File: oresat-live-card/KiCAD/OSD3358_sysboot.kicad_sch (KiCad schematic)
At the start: 7 parts, among them J3 Conn_01x02, U7 OSD3358-512M-BSM

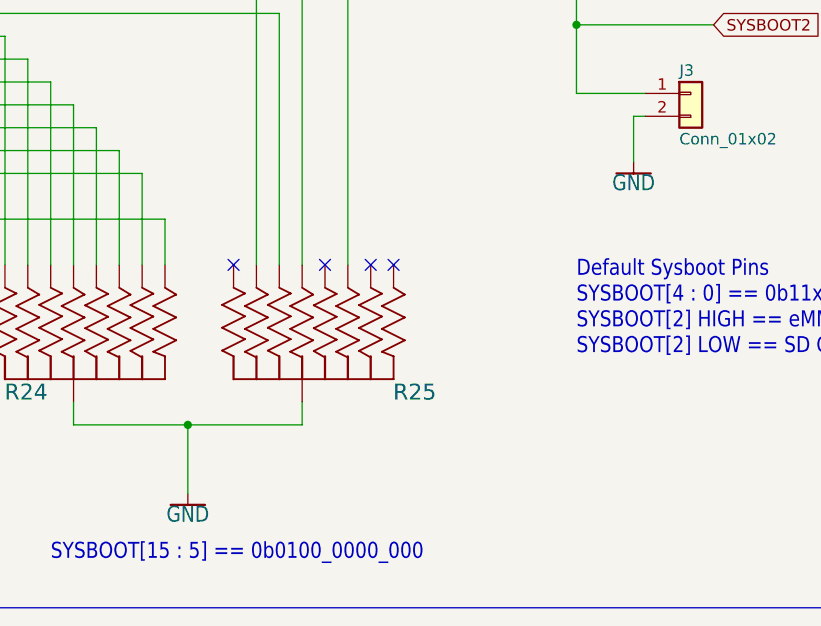
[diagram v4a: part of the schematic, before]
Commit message: completed tx/rx switch circuit and cleaned up GND references
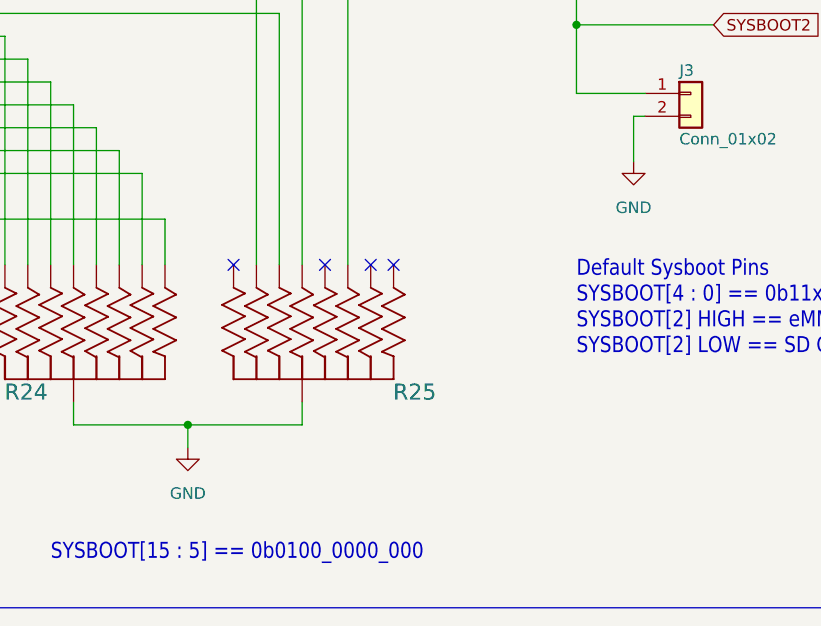
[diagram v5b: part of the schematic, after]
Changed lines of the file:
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@@
 		(title "Oresat DxWifi Card")
 		(date "2024-01-02")
-		(rev "1.3")
+		(rev "2")
 	)
 	(text "0"
@@
 	(wire
 		(pts
-			(xy 210.82 176.53) (xy 210.82 184.15)
+			(xy 210.82 176.53) (xy 210.82 179.07)
 		)
 		(stroke
@@
 	)
 	(symbol
-		(lib_id "oresat-power:GND")
-		(at 260.35 147.32 0)
-		(mirror y)
-		(unit 1)
-		(exclude_from_sim no)
-		(in_bom yes)
-		(on_board yes)
-		(dnp no)
-		(property "Reference" "#GND034"
-			(at 260.35 147.32 0)
-			(effects
-				(font
-					(size 1.27 1.27)
-				)
-				(hide yes)
-			)
-		)
-		(property "Value" "GND"
-			(at 260.35 148.59 0)
-			(effects
-				(font
-					(size 1.778 1.5113)
-				)
-				(justify top)
-			)
-		)
-		(property "Footprint" "oresat-live-card:"
-			(at 260.35 147.32 0)
-			(effects
-				(font
-					(size 1.27 1.27)
-				)
-				(hide yes)
-			)
-		)
-		(property "Datasheet" ""
-			(at 260.35 147.32 0)
-			(effects
-				(font
-					(size 1.27 1.27)
-				)
-				(hide yes)
-			)
-		)
-		(property "Description" ""
-			(at 260.35 147.32 0)
-			(effects
-				(font
-					(size 1.27 1.27)
-				)
-				(hide yes)
-			)
-		)
-		(pin "1"
-		)
-		(instances
-			(project "oresat-live-card"
-				(path "/748bdd2d-da0a-4240-ba60-0bf881d2ec56/70b8c0f4-d0a6-4f08-9b41-fcc84e804ec9"
-					(reference "#GND034")
-					(unit 1)
-				)
-			)
-		)
-	)
-	(symbol
 		(lib_id "oresat-passives:EXB-A10P391J")
 		(at 208.28 171.45 270)
@@
 	)
 	(symbol
-		(lib_id "oresat-power:GND")
-		(at 210.82 184.15 0)
-		(mirror y)
+		(lib_id "power:GND")
+		(at 260.35 147.32 0)
 		(unit 1)
 		(exclude_from_sim no)
@@
 		(on_board yes)
 		(dnp no)
-		(property "Reference" "#GND0112"
-			(at 210.82 184.15 0)
+		(fields_autoplaced yes)
+		(property "Reference" "#PWR051"
+			(at 260.35 153.67 0)
 			(effects
 				(font
@@
 		)
 		(property "Value" "GND"
-			(at 210.82 185.42 0)
-			(effects
-				(font
-					(size 1.778 1.5113)
-				)
-				(justify top)
-			)
-		)
-		(property "Footprint" "oresat-live-card:"
-			(at 210.82 184.15 0)
+			(at 260.35 152.4 0)
+			(effects
+				(font
+					(size 1.27 1.27)
+				)
+			)
+		)
+		(property "Footprint" ""
+			(at 260.35 147.32 0)
 			(effects
 				(font
@@
 		)
 		(property "Datasheet" ""
-			(at 210.82 184.15 0)
-			(effects
-				(font
-					(size 1.27 1.27)
-				)
-				(hide yes)
-			)
-		)
-		(property "Description" ""
-			(at 210.82 184.15 0)
+			(at 260.35 147.32 0)
+			(effects
+				(font
+					(size 1.27 1.27)
+				)
+				(hide yes)
+			)
+		)
+		(property "Description" "Power symbol creates a global label with name \"GND\" , ground"
+			(at 260.35 147.32 0)
 			(effects
 				(font
@@
 			(project "oresat-live-card"
 				(path "/748bdd2d-da0a-4240-ba60-0bf881d2ec56/70b8c0f4-d0a6-4f08-9b41-fcc84e804ec9"
-					(reference "#GND0112")
+					(reference "#PWR051")
 					(unit 1)
 				)
+			)
+		)
+	)
+	(symbol
+		(lib_id "power:GND")
+		(at 210.82 179.07 0)
+		(unit 1)
+		(exclude_from_sim no)
+		(in_bom yes)
+		(on_board yes)
+		(dnp no)
+		(fields_autoplaced yes)
+		(property "Reference" "#PWR050"
+			(at 210.82 185.42 0)
+			(effects
+				(font
+					(size 1.27 1.27)
+				)
+				(hide yes)
+			)
+		)
+		(property "Value" "GND"
+			(at 210.82 184.15 0)
+			(effects
+				(font
+					(size 1.27 1.27)
+				)
+			)
+		)
+		(property "Footprint" ""
+			(at 210.82 179.07 0)
+			(effects
+				(font
+					(size 1.27 1.27)
+				)
+				(hide yes)
+			)
+		)
+		(property "Datasheet" ""
+			(at 210.82 179.07 0)
+			(effects
+				(font
+					(size 1.27 1.27)
+				)
+				(hide yes)
+			)
+		)
+		(property "Description" "Power symbol creates a global label with name \"GND\" , ground"
+			(at 210.82 179.07 0)
+			(effects
+				(font
+					(size 1.27 1.27)
+				)
+				(hide yes)
+			)
+		)
+		(pin "1"
+		)
+		(instances
+			(project "oresat-live-card"
+				(path "/748bdd2d-da0a-4240-ba60-0bf881d2ec56/70b8c0f4-d0a6-4f08-9b41-fcc84e804ec9"
+					(reference "#PWR050")
+					(unit 1)
+				)

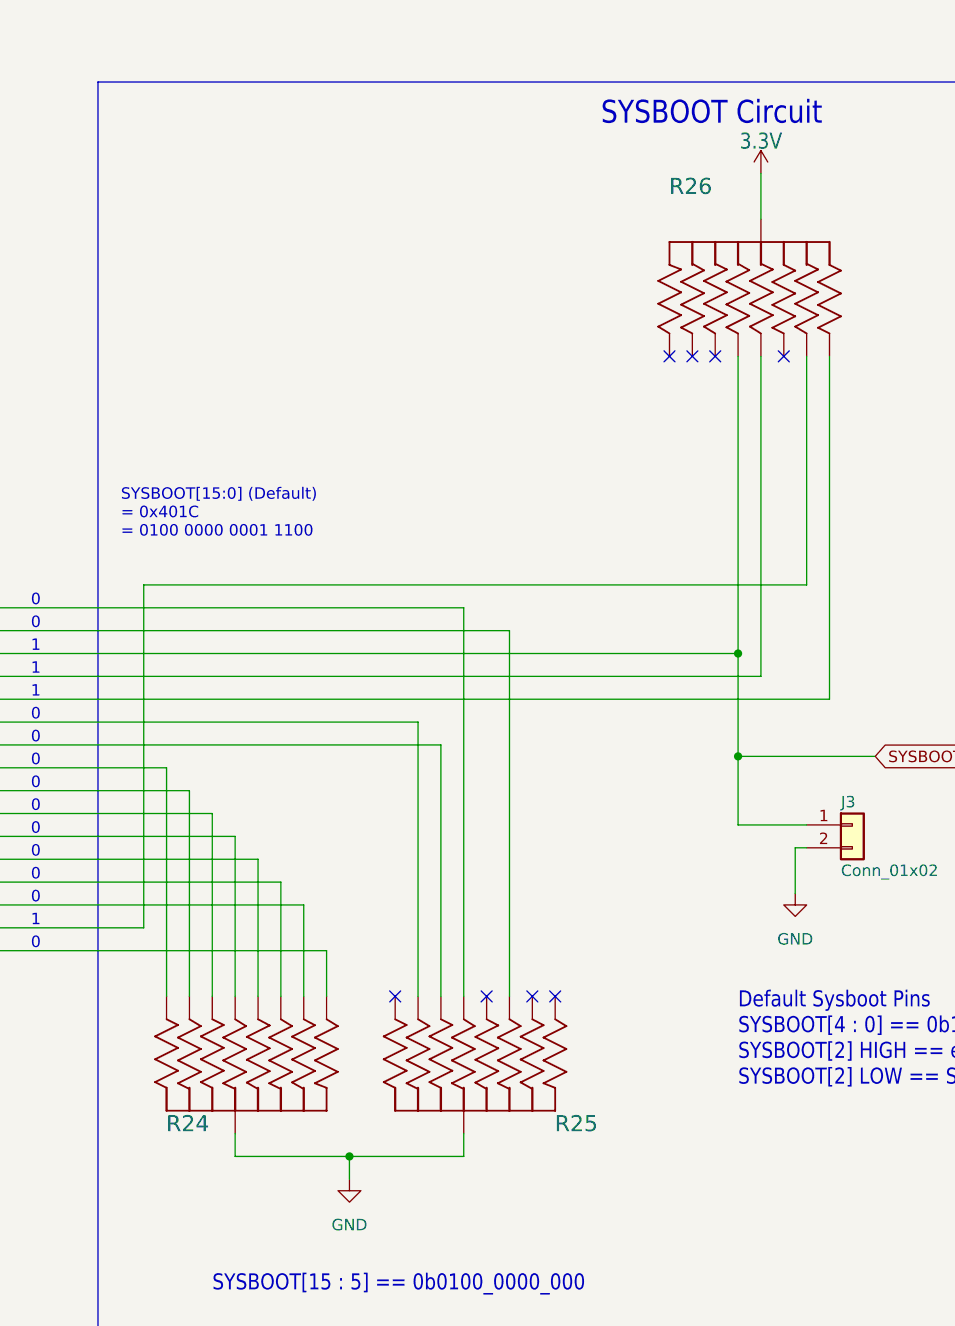
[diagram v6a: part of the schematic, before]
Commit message: Fixed up schematic as best as possible. There were a lot of issues with local paths being referenced, and EAGLE import libraries. Fixed all of those, as well as fixed some oresat-kicad IC symbols (bad direction pins) and I think we're now OK. Also updated card outline for two RF (LEFT) connectors.  Still missing two packages, but we'll deal with that later.
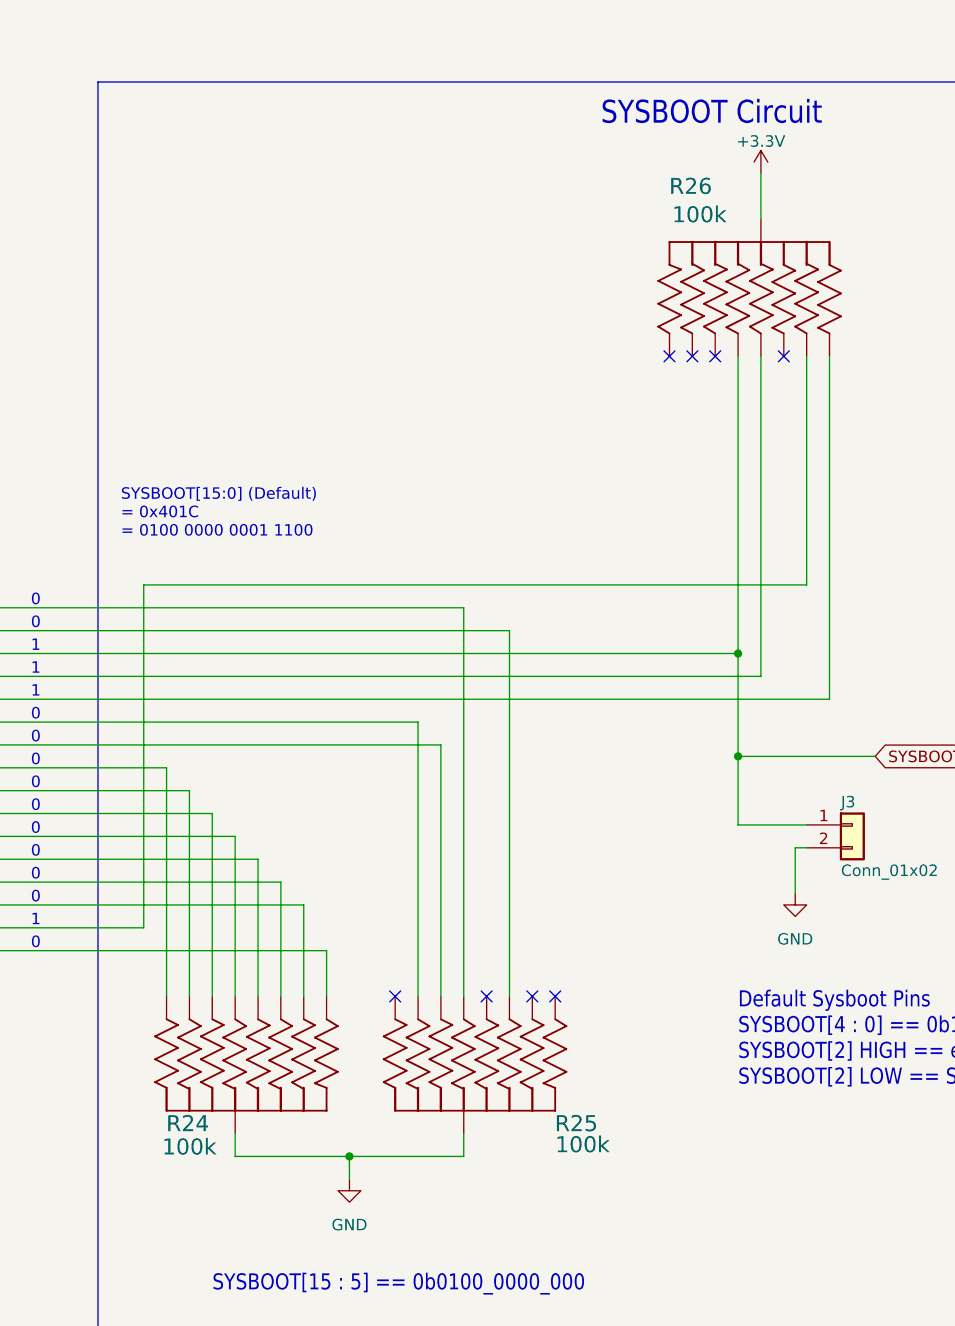
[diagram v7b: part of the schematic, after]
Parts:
- R24, R25, R26: value EXB-A10P104J -> 100k; DPN (none) -> U7104CT-ND; MFR (none) -> Panasonic
- U7: DPN (none) -> 1676-1002-ND; MFR (none) -> Octavo Systems
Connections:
- net 3.3V renamed +3.3V
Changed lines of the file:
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@@
 			)
 		)
-		(property "Value" "EXB-A10P104J"
-			(at 243.7892 92.6084 0)
+		(property "Value" "100k"
+			(at 252.73 70.866 90)
 			(effects
 				(font
@@
 				)
 				(justify left bottom)
-				(hide yes)
 			)
 		)
@@
 		(property "MPN" "EXB-A10P104J"
 			(at 246.38 74.93 0)
+			(effects
+				(font
+					(size 1.27 1.27)
+				)
+				(hide yes)
+			)
+		)
+		(property "DPN" "U7104CT-ND "
+			(at 246.38 74.93 90)
+			(effects
+				(font
+					(size 1.27 1.27)
+				)
+				(hide yes)
+			)
+		)
+		(property "MFR" "Panasonic "
+			(at 246.38 74.93 90)
 			(effects
 				(font
@@
 			)
 		)
+		(property "DPN" "1676-1002-ND "
+			(at 139.7 143.51 0)
+			(effects
+				(font
+					(size 1.27 1.27)
+				)
+				(hide yes)
+			)
+		)
+		(property "MFR" "Octavo Systems "
+			(at 139.7 143.51 0)
+			(effects
+				(font
+					(size 1.27 1.27)
+				)
+				(hide yes)
+			)
+		)
 		(pin "C10"
 		)
@@
 			)
 		)
-		(property "Value" "EXB-A10P104J"
-			(at 210.8708 153.7716 0)
+		(property "Value" "100k"
+			(at 189.992 176.53 90)
 			(effects
 				(font
@@
 				)
 				(justify left bottom)
-				(hide yes)
 			)
 		)
@@
 		(property "MPN" "EXB-A10P104J"
 			(at 208.28 171.45 0)
+			(effects
+				(font
+					(size 1.27 1.27)
+				)
+				(hide yes)
+			)
+		)
+		(property "DPN" "U7104CT-ND "
+			(at 208.28 171.45 90)
+			(effects
+				(font
+					(size 1.27 1.27)
+				)
+				(hide yes)
+			)
+		)
+		(property "MFR" "Panasonic "
+			(at 208.28 171.45 90)
 			(effects
 				(font
@@
 	)
 	(symbol
-		(lib_id "oresat-power:3.3V")
+		(lib_id "power:+3.3V")
 		(at 256.54 67.31 0)
 		(unit 1)
@@
 		(on_board yes)
 		(dnp no)
-		(property "Reference" "#3V0103"
-			(at 256.54 67.31 0)
-			(effects
-				(font
-					(size 1.27 1.27)
-				)
-				(hide yes)
-			)
-		)
-		(property "Value" "3.3V"
-			(at 256.54 64.77 0)
-			(effects
-				(font
-					(size 1.778 1.5113)
-				)
-				(justify bottom)
-			)
-		)
-		(property "Footprint" "oresat-live-card:"
+		(property "Reference" "#PWR0158"
+			(at 256.54 71.12 0)
+			(effects
+				(font
+					(size 1.27 1.27)
+				)
+				(hide yes)
+			)
+		)
+		(property "Value" "+3.3V"
+			(at 256.54 63.754 0)
+			(effects
+				(font
+					(size 1.27 1.27)
+				)
+			)
+		)
+		(property "Footprint" ""
 			(at 256.54 67.31 0)
 			(effects
@@
 			)
 		)
-		(property "Description" ""
+		(property "Description" "Power symbol creates a global label with name \"+3.3V\""
 			(at 256.54 67.31 0)
 			(effects
@@
 			(project "oresat-live-card"
 				(path "/748bdd2d-da0a-4240-ba60-0bf881d2ec56/70b8c0f4-d0a6-4f08-9b41-fcc84e804ec9"
-					(reference "#3V0103")
+					(reference "#PWR0158")
 					(unit 1)
 				)
@@
 			)
 		)
-		(property "Value" "EXB-A10P104J"
-			(at 236.2708 153.7716 0)
+		(property "Value" "100k"
+			(at 233.68 176.276 90)
 			(effects
 				(font
@@
 				)
 				(justify left bottom)
-				(hide yes)
 			)
 		)
@@
 		(property "MPN" "EXB-A10P104J"
 			(at 233.68 171.45 0)
+			(effects
+				(font
+					(size 1.27 1.27)
+				)
+				(hide yes)
+			)
+		)
+		(property "DPN" "U7104CT-ND "
+			(at 233.68 171.45 90)
+			(effects
+				(font
+					(size 1.27 1.27)
+				)
+				(hide yes)
+			)
+		)
+		(property "MFR" "Panasonic "
+			(at 233.68 171.45 90)
 			(effects
 				(font
@@
 			)
 		)
-		(property "Description" ""
+		(property "Description" "Generic connector, single row, 01x02, script generated (kicad-library-utils/schlib/autogen/connector/)"
 			(at 266.7 139.7 0)
 			(effects
@@
 		(dnp no)
 		(fields_autoplaced yes)
-		(property "Reference" "#PWR051"
+		(property "Reference" "#PWR51"
 			(at 260.35 153.67 0)
 			(effects
@@
 			(project "oresat-live-card"
 				(path "/748bdd2d-da0a-4240-ba60-0bf881d2ec56/70b8c0f4-d0a6-4f08-9b41-fcc84e804ec9"
-					(reference "#PWR051")
+					(reference "#PWR51")
 					(unit 1)
 				)
@@
 		(dnp no)
 		(fields_autoplaced yes)
-		(property "Reference" "#PWR050"
+		(property "Reference" "#PWR50"
 			(at 210.82 185.42 0)
 			(effects
@@
 			(project "oresat-live-card"
 				(path "/748bdd2d-da0a-4240-ba60-0bf881d2ec56/70b8c0f4-d0a6-4f08-9b41-fcc84e804ec9"
-					(reference "#PWR050")
+					(reference "#PWR50")
 					(unit 1)
 				)
